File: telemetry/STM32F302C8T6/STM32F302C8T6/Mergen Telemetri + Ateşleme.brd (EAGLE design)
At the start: 49.7 x 87.2 mm, 91 parts, among them J2 U.FL, Q2 IRLML6344TRPBF, Q3 IRLML6344TRPBF, U2 BMP280, U3 MPU-6050, U4 L86, U6 AMS1117-3.3, U7 AMS1117-3.3, Y2 ABM3B-26.000MHZ-10-1-U-T

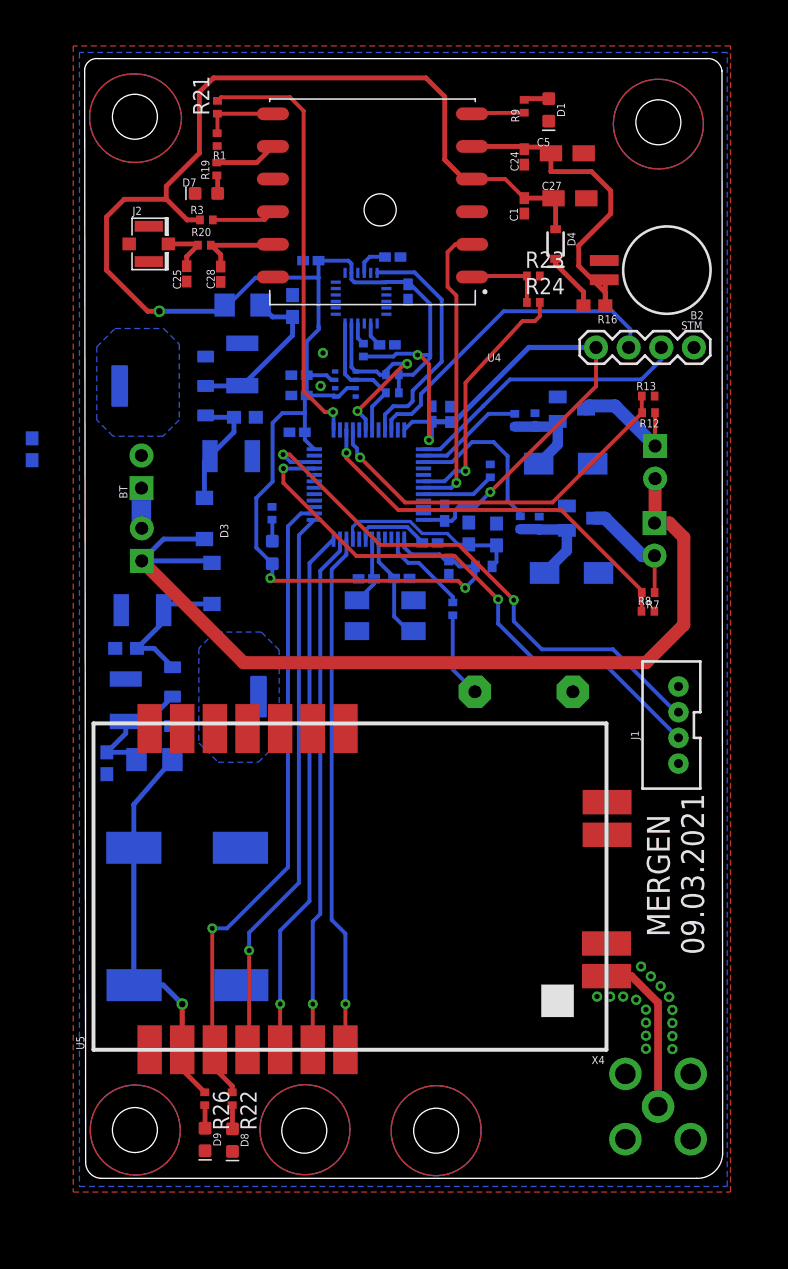
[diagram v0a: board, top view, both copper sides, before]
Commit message: New version of boards with new controller was designed
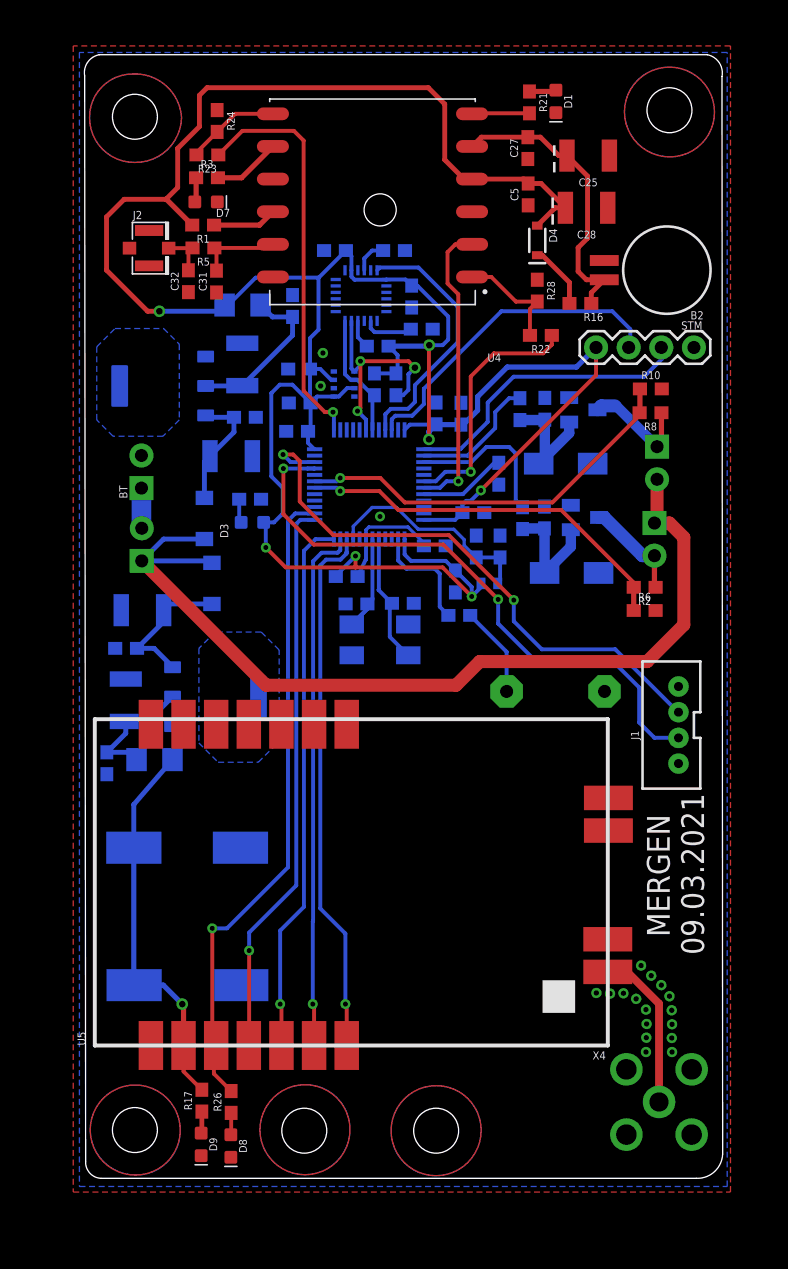
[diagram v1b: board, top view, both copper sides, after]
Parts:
- removed C1, C24: 100nF, rcl:C0402K
- removed C33, C34: 0.1uF, rcl:C0402K
- removed C35: 4.7uF, rcl:C0402K
- removed R12: 10k, rcl:R0402
- removed R13: 3k3, rcl:R0402
- removed R14: 20, rcl:R0402
- removed R15: 4.7K, rcl:R0402
- removed U1: (no value), STM32F303:LQFP48-7X7MM
- added C19: 25pF, SparkFun-Capacitors:0603
- added C20: 2.2nF, SparkFun-Capacitors:0603
- added C21, C22: 0.1uF, SparkFun-Capacitors:0603
- added R18, R29: 4k7, SparkFun-Resistors:0603
- added R27: 1k, SparkFun-Resistors:0603
- added R28: 10k, SparkFun-Resistors:0603
- added R30: 20, SparkFun-Resistors:0603
- added U8: STM32F302C8T6, STM32F302C8T6:LQFP48-7X7MM
- C10: value 100nF -> 4.7uF
- C11, C12, C13: value 0.1uF -> 100nF; device rcl:C0402K -> SparkFun-Capacitors:0603
- C14, C15, C18, C23, C31, C32: device rcl:C0402K -> SparkFun-Capacitors:0603
- C16: value 25pF -> 100nF; device rcl:C0402K -> SparkFun-Capacitors:0603
- C25: value 0.1uF -> 4.7uF; device rcl:C0402K -> SparkFun-Capacitors:EIA3528
- C27: value 10uF -> 100nF; device rcl:R/2012-12W -> SparkFun-Capacitors:0603
- C28: value 0.1uF -> 10uF; device rcl:C0402K -> SparkFun-Capacitors:EIA3528
- C30: value 2.2nF -> 0.1uF; device rcl:C0402K -> SparkFun-Capacitors:0603
- C5: value 4.7uF -> 100nF; device rcl:R/2012-12W -> SparkFun-Capacitors:0603
- R1, R2: device rcl:R0402 -> SparkFun-Resistors:0603
- R10: value 20 -> 3k3; device rcl:R0402 -> SparkFun-Resistors:0603
- R11: value 220 -> 10k; device rcl:R0402 -> SparkFun-Resistors:0603
- R17: value 1k -> 1k5; device rcl:R0402 -> SparkFun-Resistors:0603
- R19: value 100 -> 4k7; device rcl:R0402 -> SparkFun-Resistors:0603
- R20: value 0R -> 4k7; device rcl:R0402 -> SparkFun-Resistors:0603
- R21: value 680 -> 470; device rcl:R0402 -> SparkFun-Resistors:0603
- R22: value 3K3 -> 680; device rcl:R0402 -> SparkFun-Resistors:0603
- R23: value 10k -> 680; device rcl:R0402 -> SparkFun-Resistors:0603
- R24: value 680 -> 10k; device rcl:R0402 -> SparkFun-Resistors:0603
- R25: value 4.7K -> 10k; device rcl:R0402 -> SparkFun-Resistors:0603
- R26: value 1k5 -> 3k3; device rcl:R0402 -> SparkFun-Resistors:0603
- R3: value 10k -> 100; device rcl:R0402 -> SparkFun-Resistors:0603
- R4: value 4.7K -> 20; device rcl:R0402 -> SparkFun-Resistors:0603
- R5: value 4.7K -> 0; device rcl:R0402 -> SparkFun-Resistors:0603
- R6: value 4.7K -> 3k3; device rcl:R0402 -> SparkFun-Resistors:0603
- R7: value 10k -> 220; device rcl:R0402 -> SparkFun-Resistors:0603
- R8: value 3k3 -> 10k; device rcl:R0402 -> SparkFun-Resistors:0603
- R9: value 470 -> 4k7; device rcl:R0402 -> SparkFun-Resistors:0603
- moved R22 64.1 mm to (70.0, 43.6), turned to 180 degrees
- moved R17 46.0 mm to (43.6, -16.0), flipped to the top
- moved R20 33.9 mm to (70.3, 29.4), flipped to the bottom, turned to 90 degrees
- moved C10 33.5 mm to (63.8, 37.5)
- moved C25 32.6 mm to (73.7, 57.6), turned to 180 degrees
- moved C28 28.9 mm to (73.6, 53.5), turned to 180 degrees
- moved R24 28.4 mm to (44.8, 60.3), turned to 270 degrees
- moved R23 27.1 mm to (44.1, 57.7), turned to 180 degrees
- moved R6 25.9 mm to (78.1, 22.2), flipped to the top
- moved C16 25.6 mm to (58.6, 50.2)
- moved R21 24.3 mm to (69.1, 61.7), turned to 270 degrees
- moved C18 22.7 mm to (61.8, 27.2), turned to 0 degrees
- moved R9 21.9 mm to (57.3, 42.8), flipped to the bottom, turned to 180 degrees
- moved R19 21.8 mm to (58.8, 39.8), flipped to the bottom
- moved C31 19.7 mm to (44.8, 47.8), flipped to the top
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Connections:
- net 3.3V: now also C10.2, C11.2, C12.2, C13.2, C14.2, C21.2, C22.2, C23.2, C28.A, C30.2, C5.2, R1.2, R11.1, R18.2, R19.2, R9.2, U8.1, U8.24, U8.36, U8.48; no longer C1.1, C11.1, C12.1, C13.1, C14.1, C27.+, C31.1, C32.1, C33.1, C34.1, C35.1, R25.1, R3.2, R5.1, R6.1, U1.1, U1.24, U1.36, U1.48
- net 5V: now also R17.2; no longer R26.1
- net APG: now also R8.1; no longer R12.1
- net APG_F: now also R30.1, U8.38; no longer R14.1, U1.38
- net APG_S: now also R10.1, R8.2, U8.19; no longer R12.2, R13.1, U1.28
- net AUX: now also R26.2, U8.14; no longer R22.1, U1.14
- net BT0: now also R25.1, U8.44; no longer R2.1, U1.44
- net BZZR: now also R7.2, U8.2; no longer R11.1, U1.2
- net FN: now also R23.1, U8.25; no longer R21.2, U1.25
- net GND: now also C10.1, C11.1, C12.1, C13.1, C14.1, C16.1, C18.1, C19.2, C20.1, C21.1, C22.1, C23.1, C25.C, C27.1, C28.C, C30.1, C31.1, C32.1, C5.1, R10.2, R20.2, R24.1, R25.2, R27.2, R28.1, R29.2, R6.2, U8.23, U8.35, U8.47, U8.8; no longer C1.2, C11.2, C12.2, C13.2, C14.2, C16.2, C18.2, C23.2, C24.2, C25.2, C27.-, C28.2, C30.2, C31.2, C32.2, C33.2, C34.2, C35.2, C5.-, R1.2, R13.2, R15.1, R17.2, R2.2, R23.2, R4.1, R8.2, U1.23, U1.35, U1.47, U1.8
- net INT: now also U8.33; no longer U1.33
- net M0: now also U8.10; no longer U1.10
- net M1: now also U8.11; no longer U1.11
- net MAIN: now also R2.1; no longer R7.1
- net MAIN_F: now also R4.1, U8.39; no longer R10.1, U1.39
- net MAIN_S: now also R2.2, R6.1, U8.18; no longer R7.2, R8.1, U1.27
- net N$10: now also R21.2; no longer R9.2
- net N$11: now also R21.1; no longer R9.1
- net N$13: now also R20.1; no longer R10.2
- net N$14: now also R17.1; no longer R26.2
- net N$15: now also R27.1; no longer R17.1
- net N$16: now also R3.2; no longer R19.2
- net N$17: now also R3.1; no longer R19.1
- net N$18: now also C16.2; no longer C18.1
- net N$19: now also C32.2, R5.2; no longer C25.1, R20.1
- net N$20: now also R23.2, R24.2; no longer R1.1, R21.1
- net N$21: now also R26.1; no longer R22.2
- net N$22: now also C20.2; no longer C30.1
- net N$3: now also R1.1; no longer R3.1
- net N$6: now also R29.1, R30.2; no longer R14.2, R15.2
- net N$8: now also R7.1; no longer R11.2
- net NRST: now also C18.2, R11.2, U8.7; no longer C23.1, U1.7
- net OSC_IN: now also C19.1, U8.5; no longer C15.1, U1.5
- net OSC_OUT: now also C15.1, U8.6; no longer C16.1, U1.6
- net PIN22: now also R9.1; no longer R25.2
- net RX1: now also U8.43; no longer U1.43
- net RX2: now also U8.13; no longer U1.13
- net RX3: now also U8.22; no longer U1.22
- net SCL: now also R19.1, U8.30; no longer R5.2, U1.30
- net SDA: now also R18.1, U8.31; no longer R6.2, U1.31
- net SWCLK: now also U8.37; no longer U1.37
- net SWDIO: now also U8.34; no longer U1.34
- net TX1: now also R22.1, U8.42; no longer R24.2, U1.42
- net TX2: now also U8.12; no longer U1.12
- net TX3: now also U8.21; no longer U1.21
- net TXD: now also R22.2, R28.2; no longer R23.1, R24.1
- net VDDA: now also U8.9; no longer U1.9
- net V_BCKP: now also C25.A, C27.2; no longer C24.1, C5.+
- net XANT: now also C31.2, R5.1; no longer C28.1, R20.2
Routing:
- net 3.3V: track 213.1 -> 218.3 mm, vias 6 -> 7
- net OSC_OUT: track 5.40 -> 9.92 mm
- net NRST: track 5.76 -> 9.13 mm
- net V_BCKP: track 26.1 -> 22.8 mm
- net TX3: track 43.6 -> 46.6 mm
- net SCL: track 15.6 -> 18.3 mm, vias 2 -> 3
- net TXD: track 6.36 -> 8.74 mm
- net N$6: track 7.46 -> 9.78 mm
- net VDDA: track 14.9 -> 17.0 mm
- net N$22: track 1.94 -> 3.92 mm
- net RX3: track 42.7 -> 44.6 mm
- net FN: track 33.4 -> 31.6 mm
- net INT: track 18.5 -> 20.3 mm
- net N$13: track 7.70 -> 9.41 mm
- net BZZR: track 7.19 -> 8.85 mm
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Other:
- board size 49.7 x 87.2 mm -> 49.7 x 87.5 mm

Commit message: Connector was changed and Preparing first order
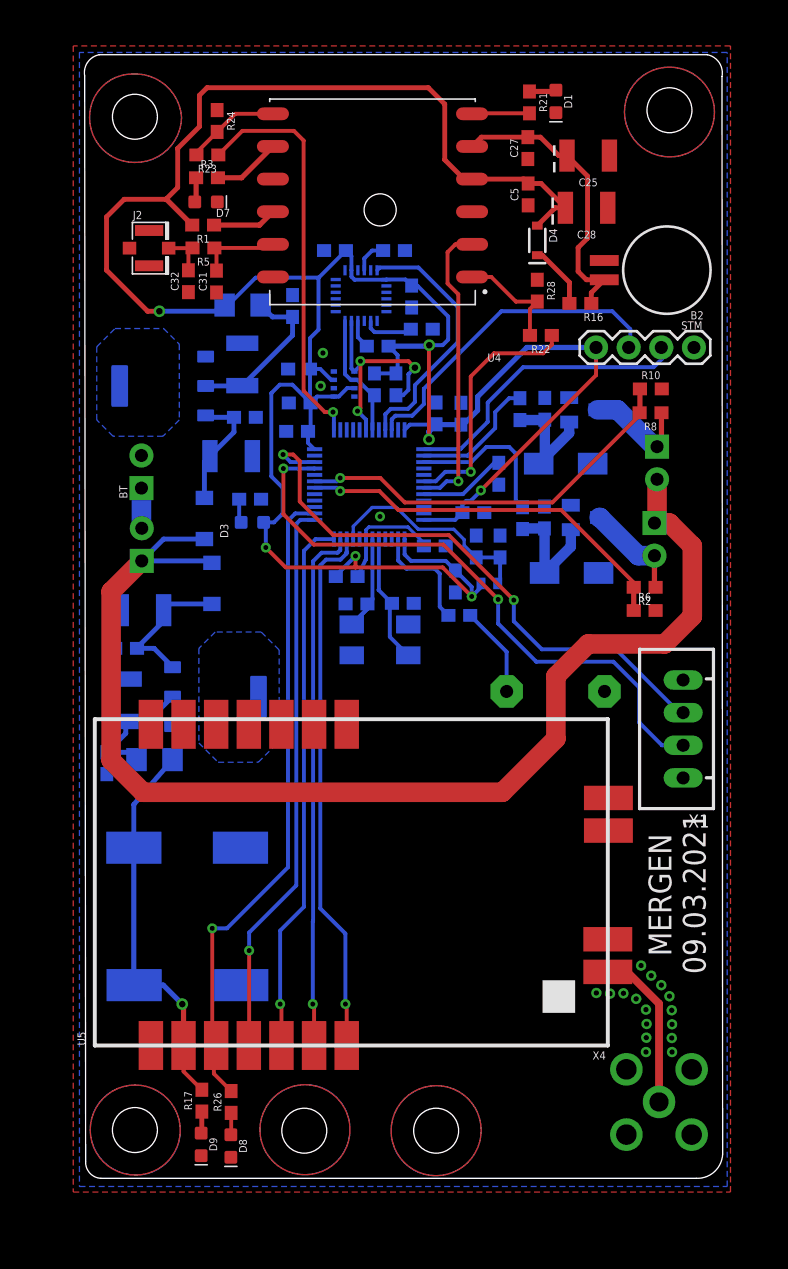
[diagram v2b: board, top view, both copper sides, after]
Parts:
- removed J1: (no value), SparkFun-Connectors:JST-4-PTH-VERT
- added X1: JST-XH-04-PIN-LONG-PAD, Rembrandt Electronics - JST XH Connectors v1-0:JST-XH-04-PACKAGE-LONG-PAD
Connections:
- net GND: now also X1.1, X1.4; no longer J1.1, J1.4
- net RX3: now also X1.3; no longer J1.3
- net TX3: now also X1.2; no longer J1.2
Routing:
- net VCC: track 72.3 -> 95.1 mm
- net TX3: track 46.6 -> 47.2 mm

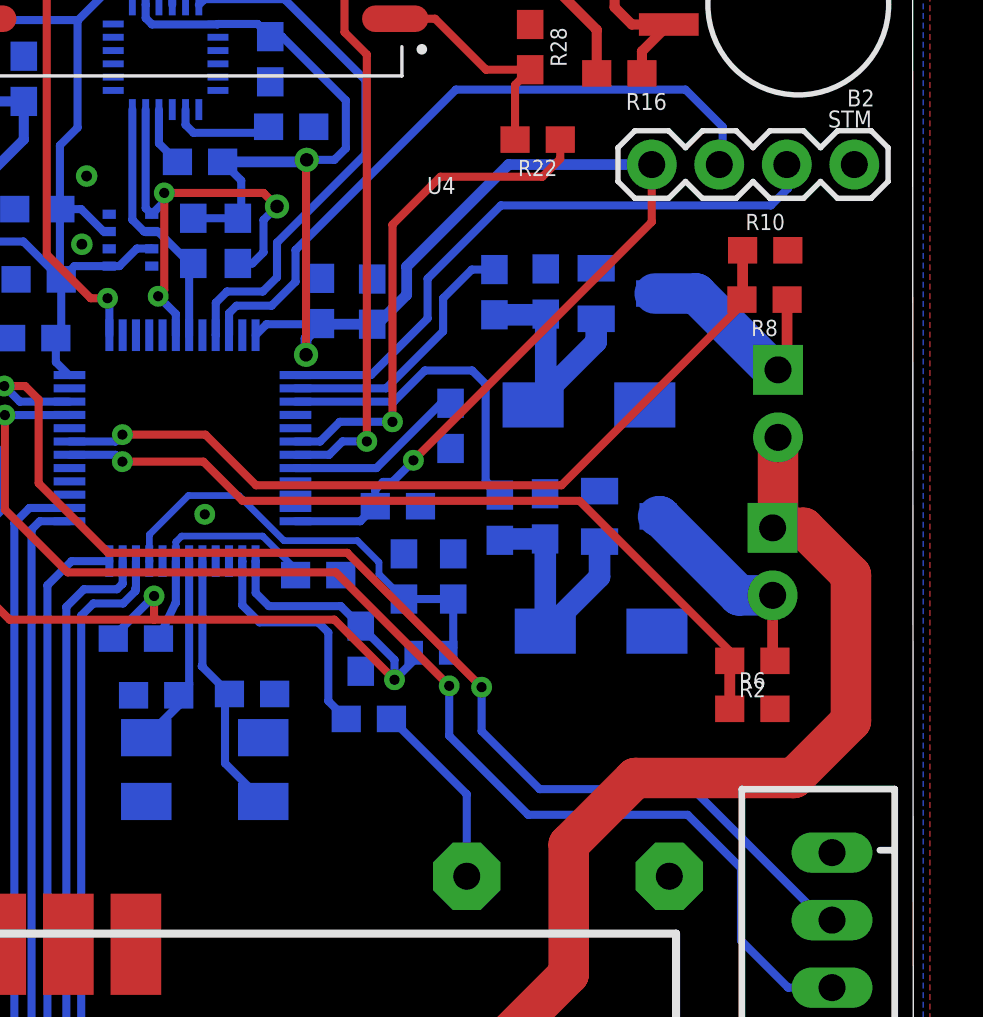
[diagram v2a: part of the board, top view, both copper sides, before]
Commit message: Polygon witdh was increased IMPORTANT
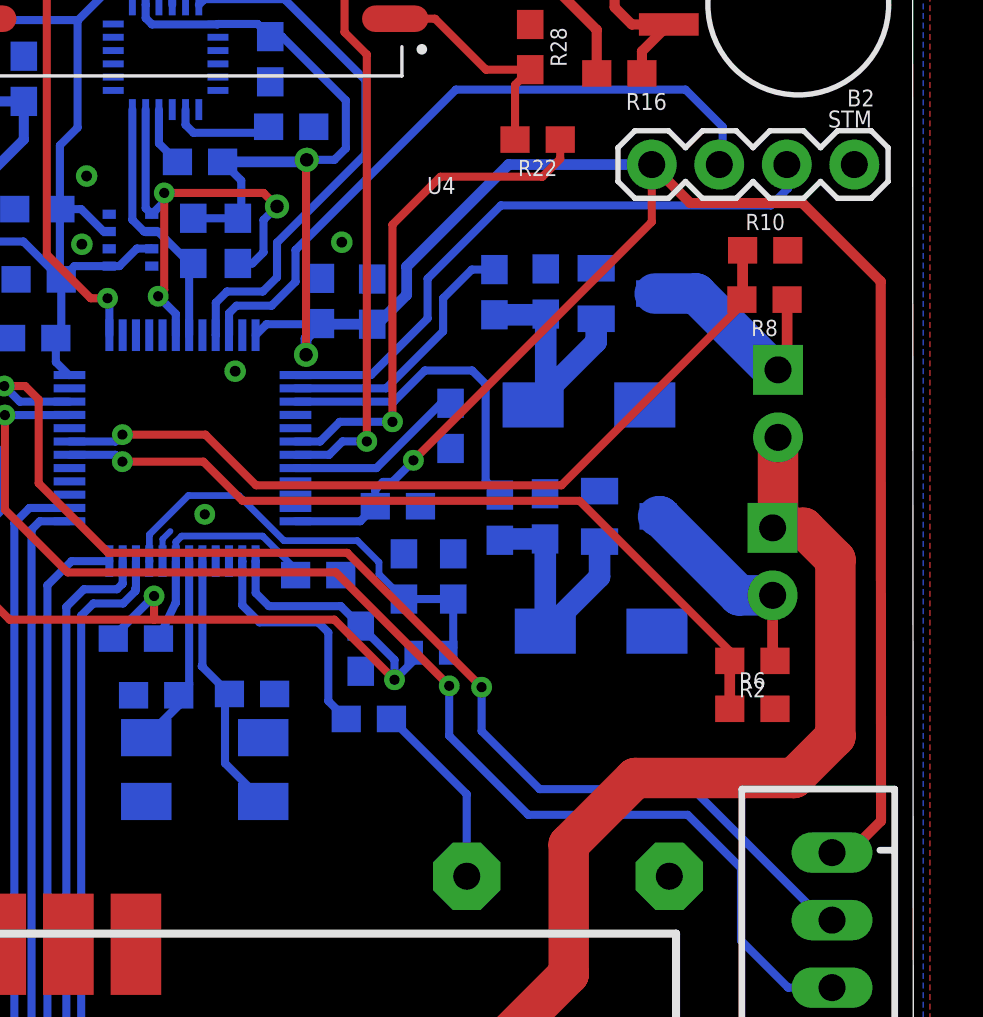
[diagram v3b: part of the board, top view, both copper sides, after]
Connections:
- net 3.3V: now also X1.4
- net GND: no longer X1.4
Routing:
- net 3.3V: track 218.3 -> 251.4 mm
- net GND: track 0.00 -> 1.25 mm, vias 19 -> 21
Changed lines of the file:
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@@
 <contactref element="SW" pad="1"/>
 <wire x1="78.867" y1="29.0068" x2="80.0354" y2="29.0068" width="1.524" layer="1"/>
-<wire x1="81.8134" y1="27.2288" x2="80.0354" y2="29.0068" width="1.524" layer="1"/>
-<wire x1="81.8134" y1="27.2288" x2="81.8134" y2="21.7424" width="1.524" layer="1"/>
-<wire x1="79.6671" y1="19.5961" x2="81.8134" y2="21.7424" width="1.524" layer="1"/>
+<wire x1="81.2292" y1="27.813" x2="80.0354" y2="29.0068" width="1.524" layer="1"/>
+<wire x1="81.2292" y1="27.813" x2="81.2292" y2="21.1582" width="1.524" layer="1"/>
+<wire x1="79.6671" y1="19.5961" x2="81.2292" y2="21.1582" width="1.524" layer="1"/>
 <wire x1="79.0702" y1="32.4104" x2="79.0702" y2="29.21" width="1.524" layer="1"/>
 <wire x1="78.867" y1="29.0068" x2="79.0702" y2="29.21" width="1.016" layer="1"/>
@@
 <contactref element="Q3" pad="2"/>
 <contactref element="Q2" pad="2"/>
-<polygon width="0" layer="16" rank="2">
+<polygon width="0.2286" layer="16" rank="2">
 <vertex x="34.1122" y="65.6336"/>
 <vertex x="34.1122" y="-22.6314"/>
@@
 <vertex x="84.5312" y="65.6336"/>
 </polygon>
-<polygon width="0" layer="1" rank="2">
+<polygon width="0.2286" layer="1" rank="2">
 <vertex x="33.6296" y="66.1416"/>
 <vertex x="33.6296" y="-23.0632"/>
@@
 <contactref element="U8" pad="8"/>
 <via x="57.5056" y="29.5148" extent="1-16" drill="0.381"/>
-<contactref element="X1" pad="4"/>
 <contactref element="X1" pad="1"/>
+<via x="58.6486" y="34.8996" extent="1-16" drill="0.4064"/>
+<via x="62.6618" y="39.751" extent="1-16" drill="0.4064"/>
+<wire x1="55.9174" y1="27.754" x2="55.9174" y2="28.587" width="0.2286" layer="16"/>
+<wire x1="55.9174" y1="28.587" x2="56.2102" y2="28.8798" width="0.2286" layer="16"/>
 </signal>
 <signal name="N$4">
@@
 <wire x1="52.392" y1="34.754" x2="52.4174" y2="34.754" width="0.3048" layer="16"/>
 <wire x1="59.4174" y1="36.254" x2="59.8292" y2="36.6658" width="0.3048" layer="16"/>
+<contactref element="X1" pad="4"/>
+<wire x1="74.3204" y1="42.672" x2="75.7682" y2="41.2242" width="0.381" layer="1"/>
+<wire x1="75.7682" y1="41.2242" x2="79.9846" y2="41.2242" width="0.381" layer="1"/>
+<wire x1="79.9846" y1="41.2242" x2="82.933334375" y2="38.275465625" width="0.381" layer="1"/>
+<wire x1="82.933334375" y1="38.275465625" x2="82.945625" y2="17.983025" width="0.381" layer="1"/>
+<wire x1="82.945625" y1="17.983025" x2="81.752" y2="16.7894" width="0.381" layer="1"/>
+<wire x1="81.752" y1="16.7894" x2="81.1022" y2="16.7894" width="0.381" layer="1"/>
 </signal>
 <signal name="VDDA">
